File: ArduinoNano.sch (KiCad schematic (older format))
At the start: 14 parts, among them IC601 ATMEGA328P-AU, IC602 FT232RL-TUBE, J601 M20-9980345, J602 USB_Connector, Y601 ECS-160-16-33B-CKM-TR

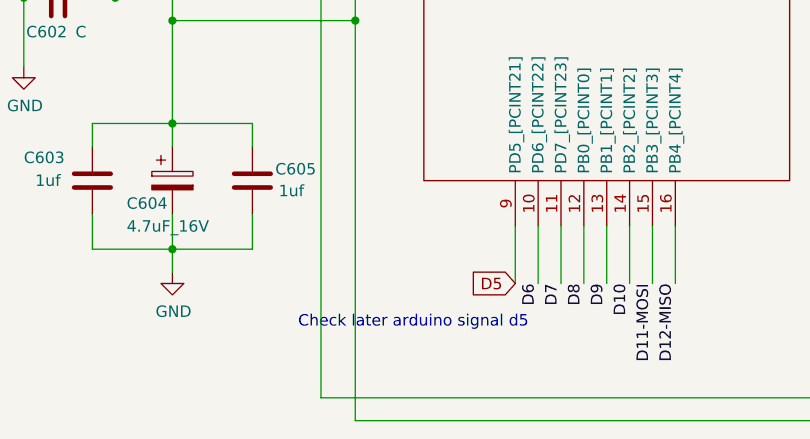
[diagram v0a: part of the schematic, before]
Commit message: adding some more labels
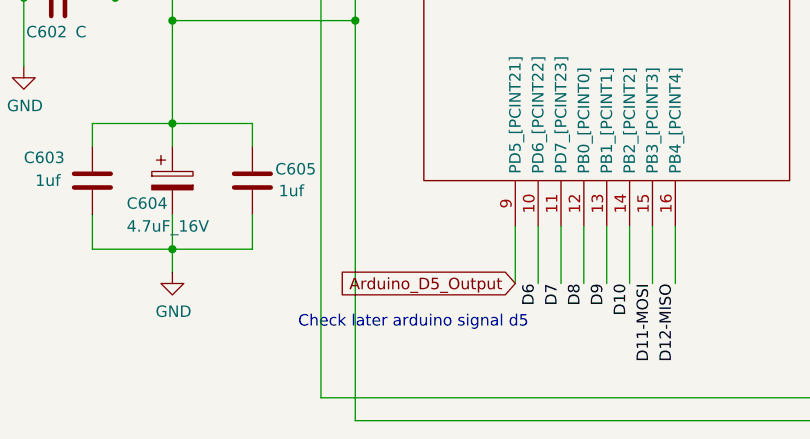
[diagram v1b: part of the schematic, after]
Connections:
- net D5 renamed Arduino_D5_Output
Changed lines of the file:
@@
 5.0V
 Text GLabel 3050 5650 0    50   Input ~ 0
-D5
+Arduino_D5_Output
 Text Notes 2100 5850 0    50   ~ 0
 Check later arduino signal d5

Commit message: FINISHED nano, power op amps
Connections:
- net A2 renamed To_Arduino_AtoD_Pos
- net A3 renamed To_Arduino_AtoD_Neg
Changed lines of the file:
@@
 Text Label 3550 2000 1    50   ~ 0
 A4
-Wire Wire Line
-	3650 2200 3650 2000
 Text Label 3650 2000 1    50   ~ 0
 A3
@@
 Text Notes 2100 5850 0    50   ~ 0
 Check later arduino signal d5
+Wire Wire Line
+	3750 2000 4700 2000
+Wire Wire Line
+	3650 1900 4700 1900
+Wire Wire Line
+	3650 1900 3650 2200
+Text GLabel 4700 1900 2    50   Input ~ 0
+To_Arduino_AtoD_Neg
+Text GLabel 4700 2000 2    50   Input ~ 0
+To_Arduino_AtoD_Pos
 $EndSCHEMATC

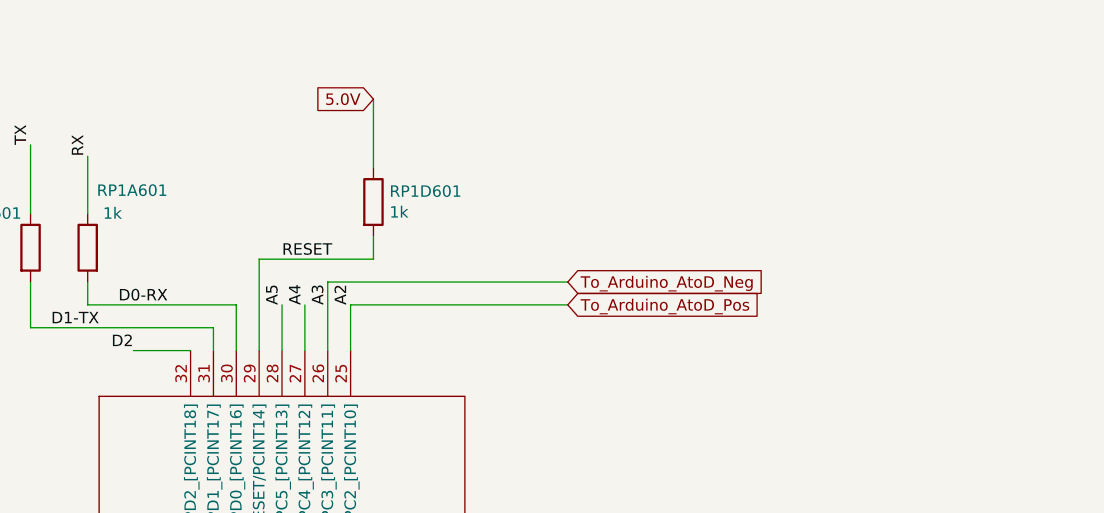
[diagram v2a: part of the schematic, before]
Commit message: made butterfly a global label, connected SDA & SCL
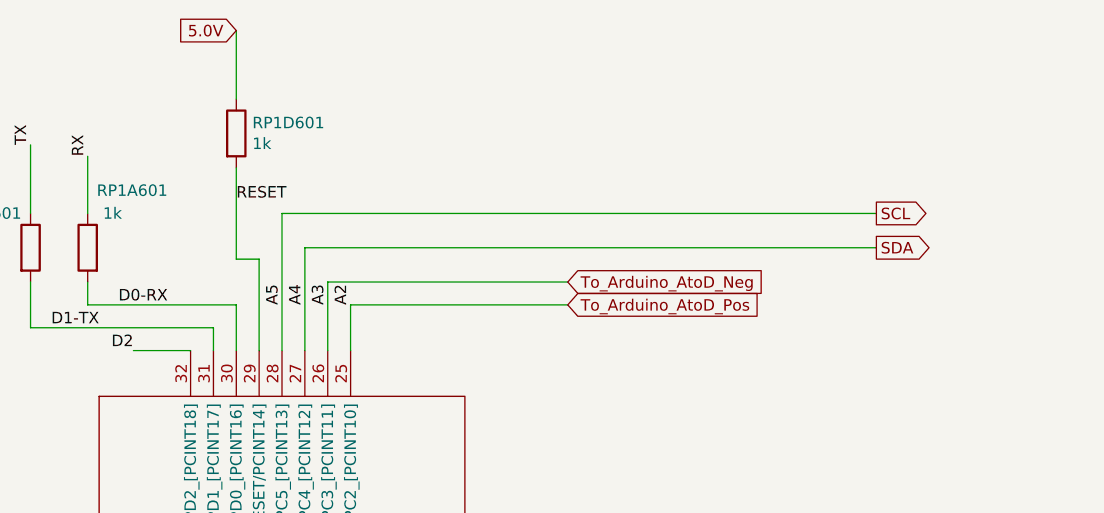
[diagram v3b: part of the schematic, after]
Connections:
- net A4 renamed SDA
- net A5 renamed SCL
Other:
- moved on the sheet: RP1D601
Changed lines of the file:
@@
 Text Label 2800 2200 2    50   ~ 0
 D2
-Wire Wire Line
-	3450 2200 3450 2000
 Text Label 3450 2000 1    50   ~ 0
 A5
-Wire Wire Line
-	3550 2200 3550 2000
 Text Label 3550 2000 1    50   ~ 0
 A4
@@
 	3350 1800 3350 2200
 Wire Wire Line
-	3350 1800 3850 1800
-Wire Wire Line
-	3850 1800 3850 1700
+	3350 1800 3250 1800
+Wire Wire Line
+	3250 1800 3250 1400
 $Comp
 L Device:R RP1D601
 U 1 1 60CE678B
-P 3850 1550
-F 0 "RP1D601" H 3920 1596 50  0000 L CNN
-F 1 "1k" H 3920 1505 50  0000 L CNN
-F 2 "Resistor_SMD:R_0402_1005Metric" V 3780 1550 50  0001 C CNN
-F 3 "~" H 3850 1550 50  0001 C CNN
-	1    3850 1550
-	1    0    0    -1
-$EndComp
-Text Label 3450 1800 0    50   ~ 0
+P 3250 1250
+F 0 "RP1D601" H 3320 1296 50  0000 L CNN
+F 1 "1k" H 3320 1205 50  0000 L CNN
+F 2 "Resistor_SMD:R_0402_1005Metric" V 3180 1250 50  0001 C CNN
+F 3 "~" H 3250 1250 50  0001 C CNN
+	1    3250 1250
+	1    0    0    -1
+$EndComp
+Text Label 3250 1550 0    50   ~ 0
 RESET
 $Comp
@@
 	6800 5300 6800 5600
 Wire Wire Line
-	3850 1100 3850 1400
+	3250 800  3250 1100
 Text GLabel 8950 5950 0    50   Input ~ 0
 5.0V
 Text GLabel 6800 5300 0    50   Input ~ 0
 5.0V
-Text GLabel 3850 1100 0    50   Input ~ 0
+Text GLabel 3250 800  0    50   Input ~ 0
 5.0V
 Text GLabel 1550 4150 1    50   Input ~ 0
@@
 Text GLabel 4700 2000 2    50   Input ~ 0
 To_Arduino_AtoD_Pos
+Text GLabel 6050 1750 2    50   Output ~ 0
+SDA
+Text GLabel 6050 1600 2    50   Output ~ 0
+SCL
+Wire Wire Line
+	3450 1600 6050 1600
+Wire Wire Line
+	3450 1600 3450 2200
+Wire Wire Line
+	6050 1750 3550 1750
+Wire Wire Line
+	3550 1750 3550 2200
 $EndSCHEMATC

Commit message: connect all grounds? maybe?
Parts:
- removed C604: 4.7uF_16V, Capacitor_SMD:C_0402_1005Metric, symbol Device:CP
- removed IC601: ATMEGA328P-AU, footprint libraries:QFP80P900X900X120-32N, symbol ATMEGA328P-AU:ATMEGA328P-AU
- added IC601: ATMEGA328PB-AN, footprint libraries:QFP80P900X900X120-32N, symbol ATMEGA328PB-AN:ATMEGA328PB-AN
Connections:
- net 5.0V: now also IC601.18 (AVCC), IC601.4 (VCC)
- net A0: now also IC601.23 (PC0_(ADC0/PTCY/MISO1))
- net A1: now also IC601.24 (PC1_(ADC1/PTCY/SCK1))
- net A6: now also IC601.19 (PE2_(ADC6/PTCY/ICP3/SS1))
- net A7: now also IC601.22 (PE3_(ADC7/PTCY/T3/MOSI1))
- net Arduino_D5_Output: now also IC601.9 ((OC0B/T1/PTCXY)_PD5)
- net D0-RX: now also IC601.30 (PD0_(PTCXY/OC3A/RXD0))
- net D1-TX: now also IC601.31 (PD1_(PTCXY/OC4A/TXD0))
- net D10: now also IC601.14 ((~SS0~/OC1B/PTCXY)_PB2)
- net D11-MOSI: now also IC601.15 ((MOSI0/TXD1/OC2A/PTCXY)_PB3)
- net D12-MISO: now also IC601.16 ((MISO0/RXD1/PTCXY)_PB4)
- net D13-SCK: now also IC601.17 (PB5_(PTCXY/XCK1/SCK0))
- net D2: now also IC601.32 (PD2_(PTCXY/INT0/OC3B/OC4B))
- net D3: now also IC601.1 ((OC2B/INT1/PTCXY)_PD3)
- net D4: now also IC601.2 ((XCK0/T0/PTCXY)_PD4)
- net D6: now also IC601.10 ((OC0A/PTCXY/AIN0)_PD6)
- net D7: now also IC601.11 ((PTCXY/AIN1)_PD7)
- net D8: now also IC601.12 ((ICP1/CLKO/PTCXY)_PB0)
- net D9: now also IC601.13 ((OC1A/PTCXY)_PB1)
- net GND: now also C601.1, Y601.1 (IN/OUT), IC601.21 (GND_2), IC601.5 (GND_1), IC601.7 ((XTAL1/TOSC1)_PB6); no longer Y601.4 (GND_2)
- net RESET: now also IC601.29 (PC6_(~RESET))
- net SCL: now also IC601.28 (PC5_(ADC5/PTCY/SCL0))
- net SDA: now also IC601.27 (PC4_(ADC4/PTCY/SDA0))
- net To_Arduino_AtoD_Neg: now also IC601.26 (PC3_(ADC3/PTCY))
- net To_Arduino_AtoD_Pos: now also IC601.25 (PC2_(ADC2/PTCY))
- net at C602.1, Y601.3 (OUT/IN): now also IC601.8 ((XTAL2/TOSC2)_PB7)
- net at C606.1: now also IC601.20 (AREF)
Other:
- note removed: "Check later arduino signal d5"
- moved on the sheet: C601, C602, C603, C605, C606, IC602, J601, J602, RP1A601, RP1B601, RP1D601, Y601

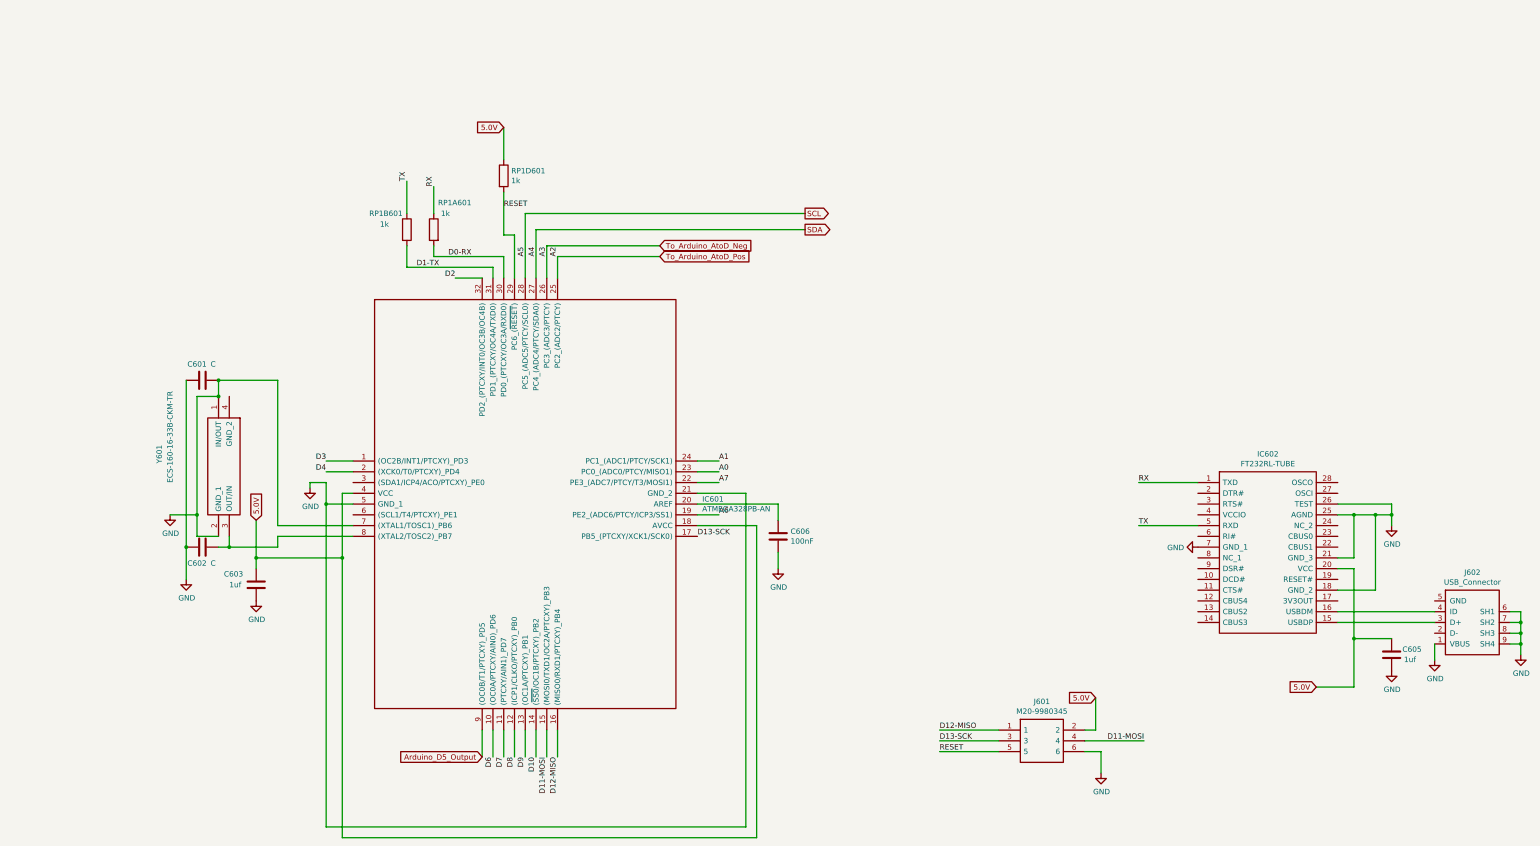
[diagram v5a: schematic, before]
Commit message: finished everything. notes: thick traces, gnd pours, keep outs/pwr plane, DRC Errors
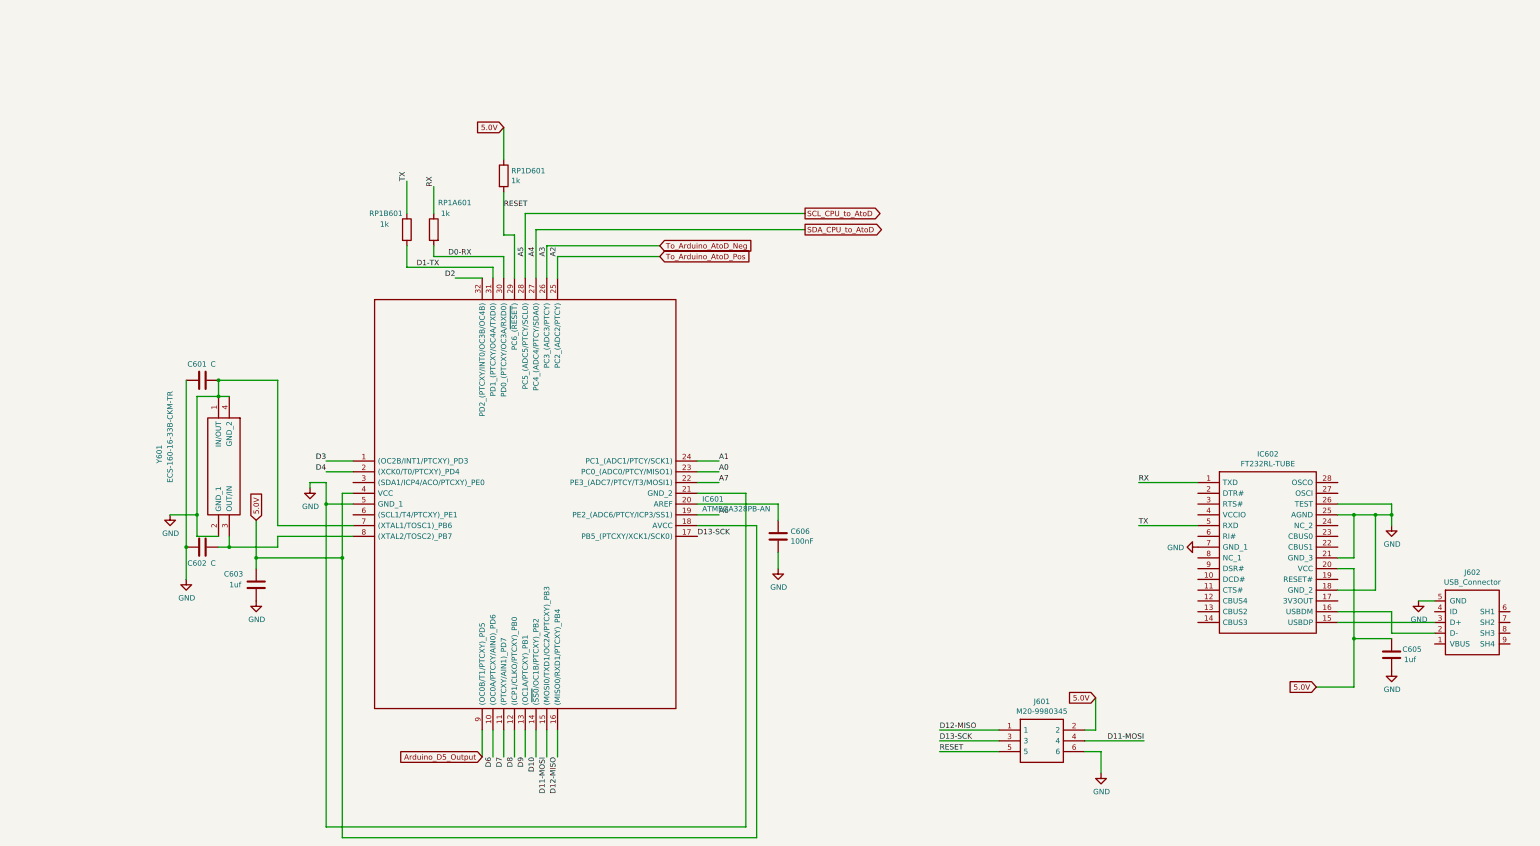
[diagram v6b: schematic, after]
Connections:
- net GND: now also J602.5 (GND), Y601.4 (GND_2); no longer J602.1 (VBUS), J602.6 (SH1), J602.7 (SH2), J602.8 (SH3), J602.9 (SH4)
- net at J602.2 (D-): now also IC602.16 (USBDM)
- net at J602.4 (ID): no longer IC602.16 (USBDM)
- net SCL renamed SCL_CPU_to_AtoD
- net SDA renamed SDA_CPU_to_AtoD
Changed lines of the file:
@@
 	0    1    1    0
 $EndComp
-$Comp
-L New_Library_for_first_symbol:USB_Connector J602
-U 1 1 60CB0840
-P 14200 6450
-F 0 "J602" H 14200 6915 50  0000 C CNN
-F 1 "USB_Connector" H 14200 6824 50  0000 C CNN
-F 2 "footprint libraries:UX60MB5ST" H 14200 6450 50  0001 C CNN
-F 3 "" H 14200 6450 50  0001 C CNN
-	1    14200 6450
-	1    0    0    -1
-$EndComp
-Wire Wire Line
-	14550 6350 14650 6350
-Wire Wire Line
-	14650 6350 14650 6450
-Wire Wire Line
-	14550 6650 14650 6650
-Connection ~ 14650 6650
-Wire Wire Line
-	14650 6650 14650 6750
-Wire Wire Line
-	14550 6550 14650 6550
-Connection ~ 14650 6550
-Wire Wire Line
-	14650 6550 14650 6650
-Wire Wire Line
-	14550 6450 14650 6450
-Connection ~ 14650 6450
-Wire Wire Line
-	14650 6450 14650 6550
-$Comp
-L power:GND #PWR0610
-U 1 1 60CB8CFF
-P 14650 6750
-F 0 "#PWR0610" H 14650 6500 50  0001 C CNN
-F 1 "GND" H 14655 6577 50  0000 C CNN
-F 2 "" H 14650 6750 50  0001 C CNN
-F 3 "" H 14650 6750 50  0001 C CNN
-	1    14650 6750
-	1    0    0    -1
-$EndComp
-Wire Wire Line
-	12950 6350 13850 6350
 Wire Wire Line
 	12950 6450 13850 6450
-Wire Wire Line
-	13850 6650 13850 6800
 $Comp
 L power:GND #PWR0609
@@
 Wire Wire Line
 	13100 6600 13100 7050
-$Comp
-L power:GND #PWR0108
-U 1 1 60D44256
-P 13850 6800
-F 0 "#PWR0108" H 13850 6550 50  0001 C CNN
-F 1 "GND" H 13855 6627 50  0000 C CNN
-F 2 "" H 13850 6800 50  0001 C CNN
-F 3 "" H 13850 6800 50  0001 C CNN
-	1    13850 6800
-	1    0    0    -1
-$EndComp
 $Comp
 L ATMEGA328PB-AN:ATMEGA328PB-AN IC601
@@
 Wire Wire Line
 	5300 2850 5300 3250
-Wire Wire Line
-	5300 2850 5200 2850
-Wire Wire Line
-	5200 2850 5200 2450
-$Comp
-L Device:R RP1D601
-U 1 1 60CE678B
-P 5200 2300
-F 0 "RP1D601" H 5270 2346 50  0000 L CNN
-F 1 "1k" H 5270 2255 50  0000 L CNN
-F 2 "Resistor_SMD:R_0402_1005Metric" V 5130 2300 50  0001 C CNN
-F 3 "~" H 5200 2300 50  0001 C CNN
-	1    5200 2300
-	1    0    0    -1
-$EndComp
-Text Label 5200 2600 0    50   ~ 0
-RESET
 $Comp
 L ECS-160-16-33B-CKM-TR:ECS-160-16-33B-CKM-TR Y601
@@
 	2350 5650 2350 5450
 Wire Wire Line
-	2350 4350 2550 4350
-Wire Wire Line
 	2250 4200 2250 5750
 Wire Wire Line
@@
 To_Arduino_AtoD_Pos
 Text GLabel 8000 2800 2    50   Output ~ 0
-SDA
+SDA_CPU_to_AtoD
 Text GLabel 8000 2650 2    50   Output ~ 0
-SCL
+SCL_CPU_to_AtoD
 Wire Wire Line
 	5400 2650 8000 2650
@@
 Wire Wire Line
 	5600 2950 6650 2950
+Wire Wire Line
+	3550 8350 7450 8350
+Wire Wire Line
+	7450 5250 7450 8350
+Wire Wire Line
+	3550 5350 3550 8350
+Wire Wire Line
+	3700 8450 7550 8450
+Wire Wire Line
+	7550 5550 7550 8450
+Wire Wire Line
+	3700 5850 3700 8450
+Text Label 5200 2600 0    50   ~ 0
+RESET
+$Comp
+L Device:R RP1D601
+U 1 1 60CE678B
+P 5200 2300
+F 0 "RP1D601" H 5270 2346 50  0000 L CNN
+F 1 "1k" H 5270 2255 50  0000 L CNN
+F 2 "Resistor_SMD:R_0402_1005Metric" V 5130 2300 50  0001 C CNN
+F 3 "~" H 5200 2300 50  0001 C CNN
+	1    5200 2300
+	1    0    0    -1
+$EndComp
+Wire Wire Line
+	5200 2850 5200 2450
+Wire Wire Line
+	5300 2850 5200 2850
+Wire Wire Line
+	2550 4350 2650 4350
+Wire Wire Line
+	2350 4350 2550 4350
 Connection ~ 2550 4350
 Wire Wire Line
-	3550 8350 7450 8350
-Wire Wire Line
-	7450 5250 7450 8350
-Wire Wire Line
-	3550 5350 3550 8350
-Wire Wire Line
-	3700 8450 7550 8450
-Wire Wire Line
-	7550 5550 7550 8450
-Wire Wire Line
-	3700 5850 3700 8450
+	13850 6550 13450 6550
+Wire Wire Line
+	13450 6550 13450 6350
+Wire Wire Line
+	13450 6350 12950 6350
+$Comp
+L New_Library_for_first_symbol:USB_Connector J602
+U 1 1 60CB0840
+P 14200 6450
+F 0 "J602" H 14200 6915 50  0000 C CNN
+F 1 "USB_Connector" H 14200 6824 50  0000 C CNN
+F 2 "footprint libraries:UX60MB5ST" H 14200 6450 50  0001 C CNN
+F 3 "" H 14200 6450 50  0001 C CNN
+	1    14200 6450
+	1    0    0    -1
+$EndComp
+$Comp
+L power:GND #PWR?
+U 1 1 60E91EBF
+P 13700 6250
+F 0 "#PWR?" H 13700 6000 50  0001 C CNN
+F 1 "GND" H 13705 6077 50  0000 C CNN
+F 2 "" H 13700 6250 50  0001 C CNN
+F 3 "" H 13700 6250 50  0001 C CNN
+	1    13700 6250
+	1    0    0    -1
+$EndComp
+Wire Wire Line
+	13700 6250 13850 6250
 $EndSCHEMATC

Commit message: weird airwires
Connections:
- net 5.0V: now also IC602.4 (VCCIO)
- net GND: no longer C601.1, IC601.7 ((XTAL1/TOSC1)_PB6), Y601.1 (IN/OUT)
- new net: C601.1, IC601.7 ((XTAL1/TOSC1)_PB6), Y601.1 (IN/OUT)
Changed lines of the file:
@@
 	5300 2850 5200 2850
-Wire Wire Line
-	2550 4350 2650 4350
-Wire Wire Line
-	2350 4350 2550 4350
-Connection ~ 2550 4350
 Wire Wire Line
 	13850 6550 13450 6550
@@
 $EndComp
 $Comp
-L power:GND #PWR?
+L power:GND #PWR0108
 U 1 1 60E91EBF
 P 13700 6250
-F 0 "#PWR?" H 13700 6000 50  0001 C CNN
+F 0 "#PWR0108" H 13700 6000 50  0001 C CNN
 F 1 "GND" H 13705 6077 50  0000 C CNN
 F 2 "" H 13700 6250 50  0001 C CNN
@@
 Wire Wire Line
 	13700 6250 13850 6250
+Wire Wire Line
+	11650 5450 11000 5450
+Wire Wire Line
+	11000 5450 11000 4750
+Text GLabel 11000 4750 0    50   Input ~ 0
+5.0V
+Wire Wire Line
+	2350 4350 2650 4350
 $EndSCHEMATC
